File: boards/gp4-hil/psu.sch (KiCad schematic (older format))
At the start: 80 parts, among them K1 CONN_3_PWROUT, Q11 SSM6N58NU, Q12 DMP2069UFY4, Q22 DMP2069UFY4, U1 MIC2288-DFN, U20 SIP32408, U21 SIP32408, U22 SIP32408, U23 SIP32408, U24 SIP32408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

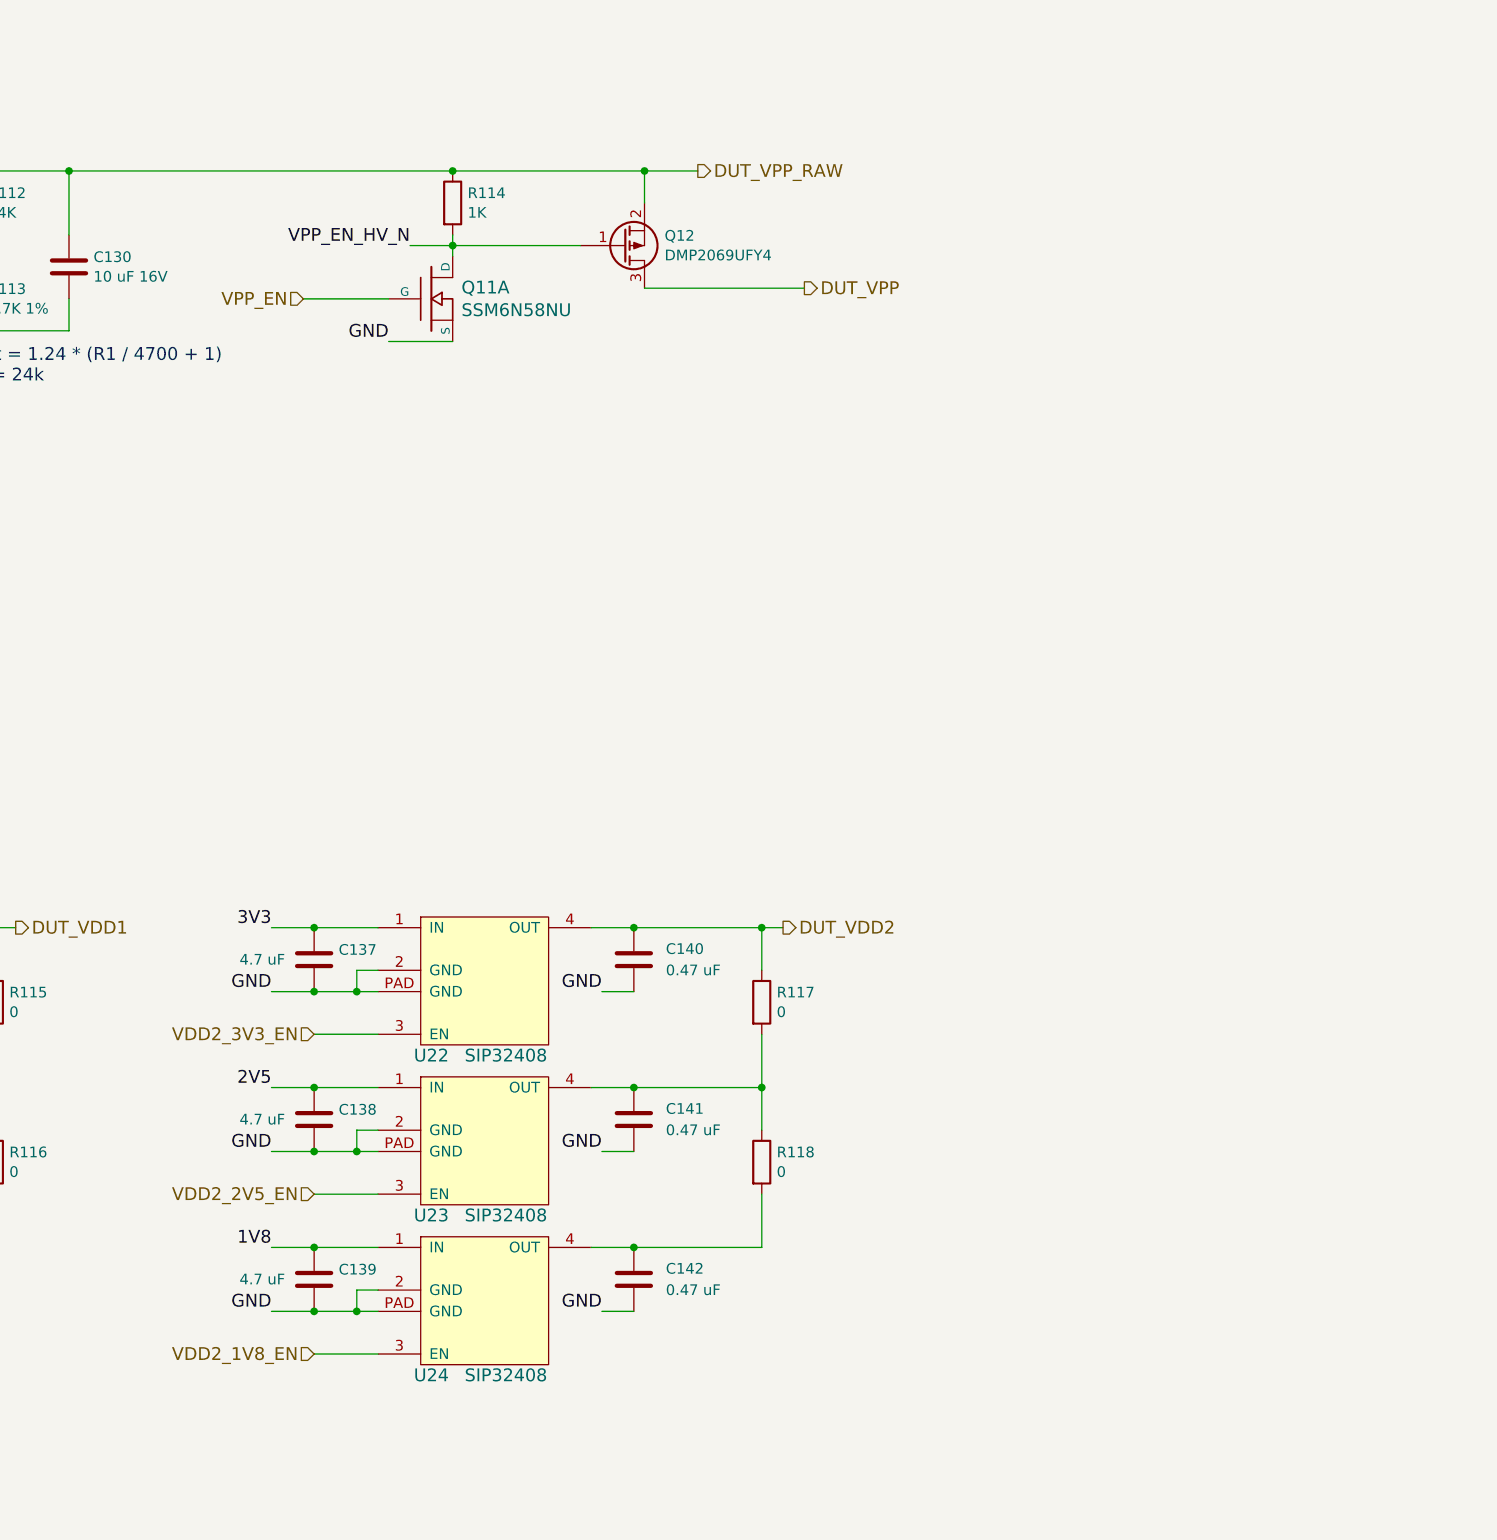
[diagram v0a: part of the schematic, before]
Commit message: Added current monitoring shunts. Began design review
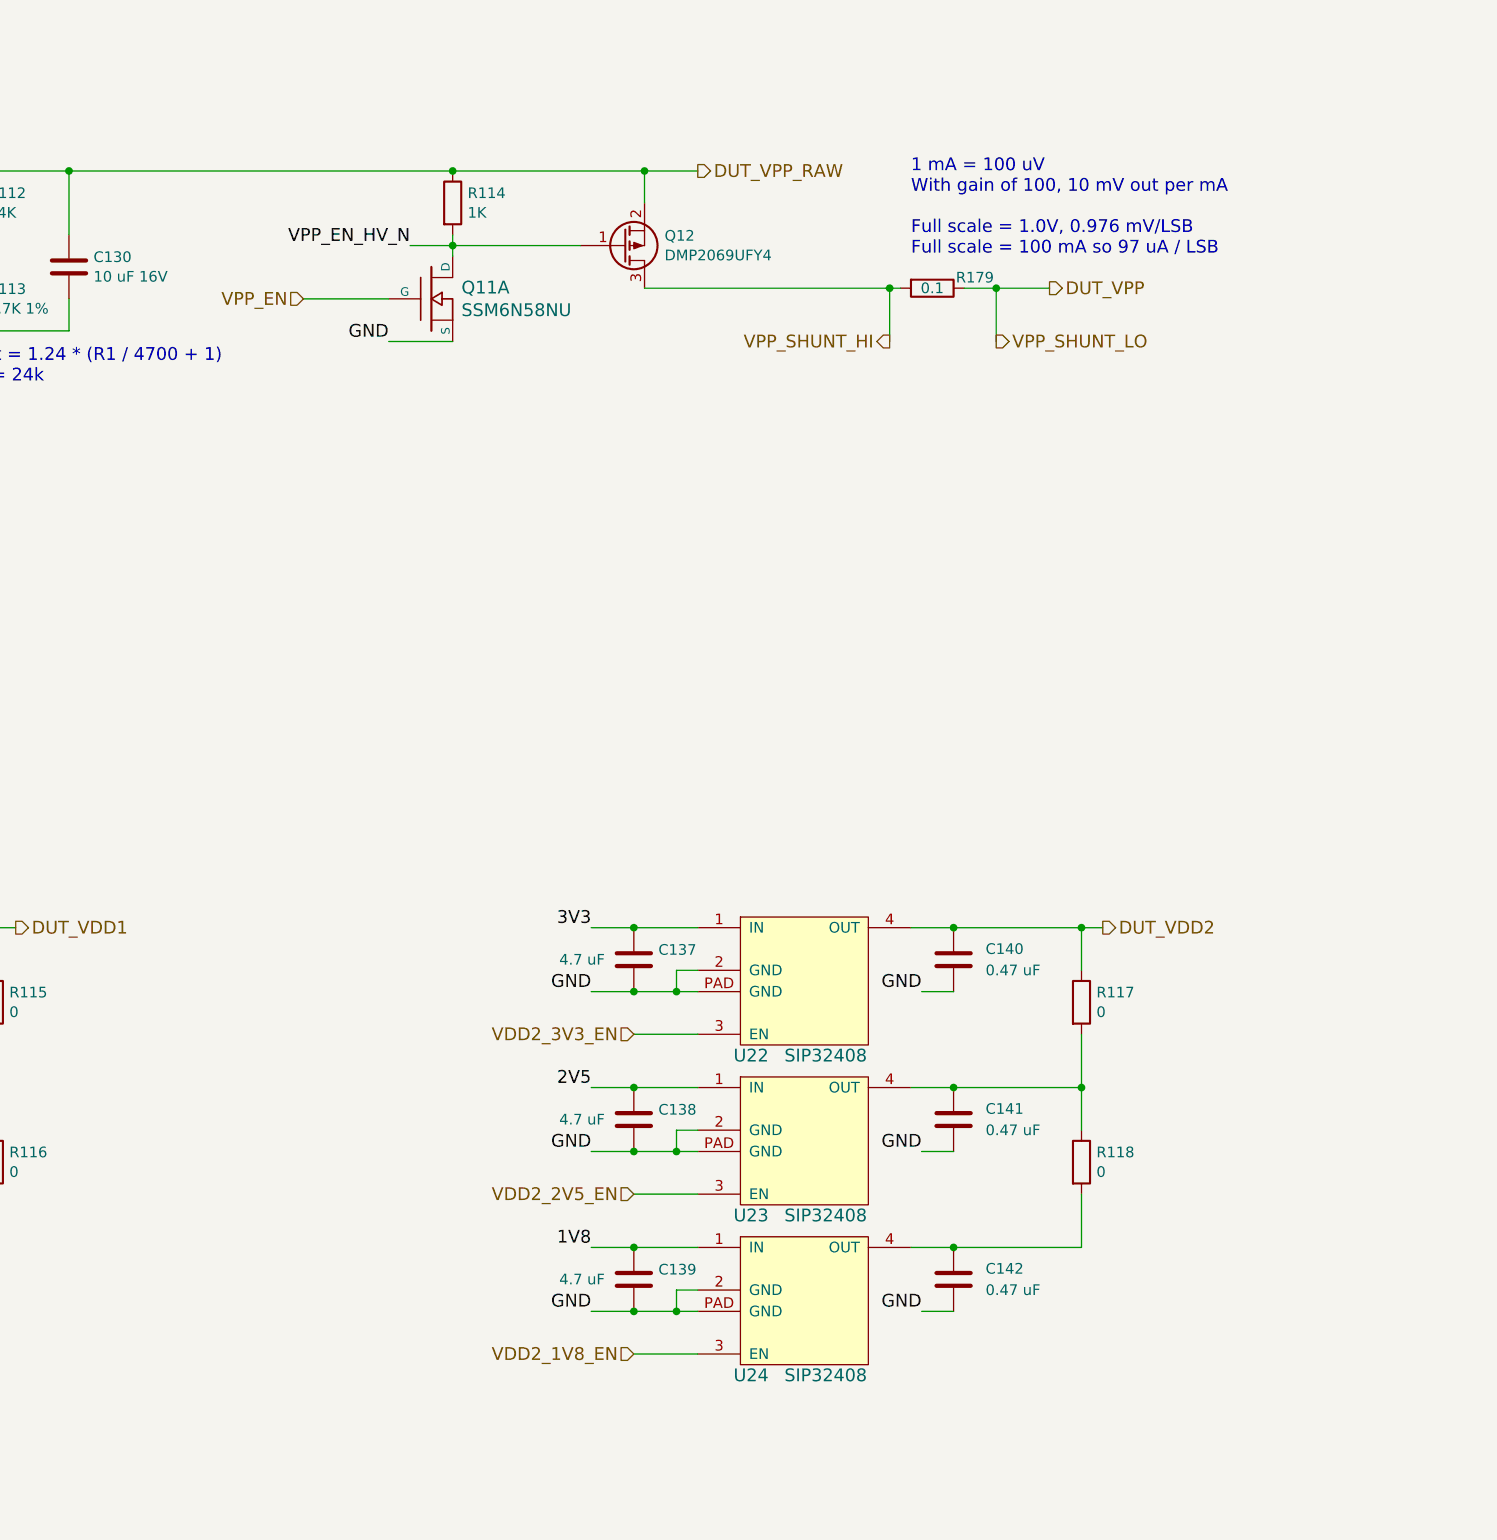
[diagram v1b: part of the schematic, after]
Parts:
- added R179: 0.1, symbol R
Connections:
- net DUT_VPP: now also R179.1; no longer Q12.3 (D)
- new net VPP_SHUNT_HI: Q12.3 (D), R179.2
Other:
- note added: "1 mA = 100 uV\nWith gain of 100, 10 mV out per mA\n\nFull scale = 1.0V, 0.976 mV/LSB\nFull scale = 100 mA so 97 uA / LSB"
- moved on the sheet: C137, C138, C139, C140, C141, C142, R117, R118, U22, U23, U24
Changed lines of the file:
@@
 Sheet 2 7
 Title "GreenPak Hardware-In-Loop Test Platform"
-Date "2016-05-17"
+Date "2016-05-18"
 Rev "0.1"
 Comp "Andrew Zonenberg"
@@
 	-1   0    0    -1
 $EndComp
-Text HLabel 13100 4550 2    60   Output ~ 0
+Text HLabel 14250 4550 2    60   Output ~ 0
 DUT_VPP
 Text HLabel 4550 9500 2    60   Output ~ 0
@@
 Text HLabel 7200 8800 0    60   Input ~ 0
 VDD1_2V5_EN
-Text HLabel 13000 7550 2    60   Output ~ 0
+Text HLabel 14500 7550 2    60   Output ~ 0
 DUT_VDD2
 $Comp
 L SIP32408 U22
 U 1 1 57415A55
-P 11300 8100
-F 0 "U22" H 11350 8050 60  0000 C CNN
-F 1 "SIP32408" H 11700 8050 60  0000 C CNN
-F 2 "" H 11300 8100 60  0000 C CNN
-F 3 "" H 11300 8100 60  0000 C CNN
-	1    11300 8100
+P 12800 8100
+F 0 "U22" H 12850 8050 60  0000 C CNN
+F 1 "SIP32408" H 13200 8050 60  0000 C CNN
+F 2 "" H 12800 8100 60  0000 C CNN
+F 3 "" H 12800 8100 60  0000 C CNN
+	1    12800 8100
 	1    0    0    -1
 $EndComp
@@
 L C C137
 U 1 1 57415A5B
-P 10800 7700
-F 0 "C137" H 10915 7746 50  0000 L CNN
-F 1 "4.7 uF" H 10450 7700 50  0000 L CNN
-F 2 "" H 10838 7550 30  0000 C CNN
-F 3 "" H 10800 7700 60  0000 C CNN
-	1    10800 7700
-	1    0    0    -1
-$EndComp
-Text Label 10600 7850 2    60   ~ 0
-GND
-Text Label 10600 7550 2    60   ~ 0
-3V3
-$Comp
-L C C140
-U 1 1 57415A63
 P 12300 7700
-F 0 "C140" H 12450 7750 50  0000 L CNN
-F 1 "0.47 uF" H 12450 7650 50  0000 L CNN
+F 0 "C137" H 12415 7746 50  0000 L CNN
+F 1 "4.7 uF" H 11950 7700 50  0000 L CNN
 F 2 "" H 12338 7550 30  0000 C CNN
 F 3 "" H 12300 7700 60  0000 C CNN
@@
 	1    0    0    -1
 $EndComp
-Text Label 12150 7850 2    60   ~ 0
-GND
-Text HLabel 10800 8050 0    60   Input ~ 0
+Text Label 12100 7850 2    60   ~ 0
+GND
+Text Label 12100 7550 2    60   ~ 0
+3V3
+$Comp
+L C C140
+U 1 1 57415A63
+P 13800 7700
+F 0 "C140" H 13950 7750 50  0000 L CNN
+F 1 "0.47 uF" H 13950 7650 50  0000 L CNN
+F 2 "" H 13838 7550 30  0000 C CNN
+F 3 "" H 13800 7700 60  0000 C CNN
+	1    13800 7700
+	1    0    0    -1
+$EndComp
+Text Label 13650 7850 2    60   ~ 0
+GND
+Text HLabel 12300 8050 0    60   Input ~ 0
 VDD2_3V3_EN
 $Comp
 L SIP32408 U24
 U 1 1 57415A75
-P 11300 9600
-F 0 "U24" H 11350 9550 60  0000 C CNN
-F 1 "SIP32408" H 11700 9550 60  0000 C CNN
-F 2 "" H 11300 9600 60  0000 C CNN
-F 3 "" H 11300 9600 60  0000 C CNN
-	1    11300 9600
+P 12800 9600
+F 0 "U24" H 12850 9550 60  0000 C CNN
+F 1 "SIP32408" H 13200 9550 60  0000 C CNN
+F 2 "" H 12800 9600 60  0000 C CNN
+F 3 "" H 12800 9600 60  0000 C CNN
+	1    12800 9600
 	1    0    0    -1
 $EndComp
@@
 L C C139
 U 1 1 57415A7B
-P 10800 9200
-F 0 "C139" H 10915 9246 50  0000 L CNN
-F 1 "4.7 uF" H 10450 9200 50  0000 L CNN
-F 2 "" H 10838 9050 30  0000 C CNN
-F 3 "" H 10800 9200 60  0000 C CNN
-	1    10800 9200
-	1    0    0    -1
-$EndComp
-Text Label 10600 9350 2    60   ~ 0
-GND
-Text Label 10600 9050 2    60   ~ 0
-1V8
-$Comp
-L C C142
-U 1 1 57415A83
 P 12300 9200
-F 0 "C142" H 12450 9250 50  0000 L CNN
-F 1 "0.47 uF" H 12450 9150 50  0000 L CNN
+F 0 "C139" H 12415 9246 50  0000 L CNN
+F 1 "4.7 uF" H 11950 9200 50  0000 L CNN
 F 2 "" H 12338 9050 30  0000 C CNN
 F 3 "" H 12300 9200 60  0000 C CNN
@@
 	1    0    0    -1
 $EndComp
-Text Label 12150 9350 2    60   ~ 0
-GND
-Text HLabel 10800 9550 0    60   Input ~ 0
+Text Label 12100 9350 2    60   ~ 0
+GND
+Text Label 12100 9050 2    60   ~ 0
+1V8
+$Comp
+L C C142
+U 1 1 57415A83
+P 13800 9200
+F 0 "C142" H 13950 9250 50  0000 L CNN
+F 1 "0.47 uF" H 13950 9150 50  0000 L CNN
+F 2 "" H 13838 9050 30  0000 C CNN
+F 3 "" H 13800 9200 60  0000 C CNN
+	1    13800 9200
+	1    0    0    -1
+$EndComp
+Text Label 13650 9350 2    60   ~ 0
+GND
+Text HLabel 12300 9550 0    60   Input ~ 0
 VDD2_1V8_EN
 $Comp
 L SIP32408 U23
 U 1 1 57415A95
-P 11300 8850
-F 0 "U23" H 11350 8800 60  0000 C CNN
-F 1 "SIP32408" H 11700 8800 60  0000 C CNN
-F 2 "" H 11300 8850 60  0000 C CNN
-F 3 "" H 11300 8850 60  0000 C CNN
-	1    11300 8850
+P 12800 8850
+F 0 "U23" H 12850 8800 60  0000 C CNN
+F 1 "SIP32408" H 13200 8800 60  0000 C CNN
+F 2 "" H 12800 8850 60  0000 C CNN
+F 3 "" H 12800 8850 60  0000 C CNN
+	1    12800 8850
 	1    0    0    -1
 $EndComp
@@
 L C C138
 U 1 1 57415A9B
-P 10800 8450
-F 0 "C138" H 10915 8496 50  0000 L CNN
-F 1 "4.7 uF" H 10450 8450 50  0000 L CNN
-F 2 "" H 10838 8300 30  0000 C CNN
-F 3 "" H 10800 8450 60  0000 C CNN
-	1    10800 8450
-	1    0    0    -1
-$EndComp
-Text Label 10600 8600 2    60   ~ 0
-GND
-Text Label 10600 8300 2    60   ~ 0
-2V5
-$Comp
-L C C141
-U 1 1 57415AA3
 P 12300 8450
-F 0 "C141" H 12450 8500 50  0000 L CNN
-F 1 "0.47 uF" H 12450 8400 50  0000 L CNN
+F 0 "C138" H 12415 8496 50  0000 L CNN
+F 1 "4.7 uF" H 11950 8450 50  0000 L CNN
 F 2 "" H 12338 8300 30  0000 C CNN
 F 3 "" H 12300 8450 60  0000 C CNN
@@
 	1    0    0    -1
 $EndComp
-Text Label 12150 8600 2    60   ~ 0
-GND
-Text HLabel 10800 8800 0    60   Input ~ 0
+Text Label 12100 8600 2    60   ~ 0
+GND
+Text Label 12100 8300 2    60   ~ 0
+2V5
+$Comp
+L C C141
+U 1 1 57415AA3
+P 13800 8450
+F 0 "C141" H 13950 8500 50  0000 L CNN
+F 1 "0.47 uF" H 13950 8400 50  0000 L CNN
+F 2 "" H 13838 8300 30  0000 C CNN
+F 3 "" H 13800 8450 60  0000 C CNN
+	1    13800 8450
+	1    0    0    -1
+$EndComp
+Text Label 13650 8600 2    60   ~ 0
+GND
+Text HLabel 12300 8800 0    60   Input ~ 0
 VDD2_2V5_EN
 Text HLabel 10750 4600 0    60   Input ~ 0
@@
 L R R117
 U 1 1 574582F9
-P 12900 7900
-F 0 "R117" H 12970 7946 50  0000 L CNN
-F 1 "0" H 12970 7854 50  0000 L CNN
-F 2 "" V 12830 7900 30  0000 C CNN
-F 3 "" H 12900 7900 30  0000 C CNN
-	1    12900 7900
+P 14400 7900
+F 0 "R117" H 14470 7946 50  0000 L CNN
+F 1 "0" H 14470 7854 50  0000 L CNN
+F 2 "" V 14330 7900 30  0000 C CNN
+F 3 "" H 14400 7900 30  0000 C CNN
+	1    14400 7900
 	1    0    0    -1
 $EndComp
@@
 L R R118
 U 1 1 5745846F
-P 12900 8650
-F 0 "R118" H 12970 8696 50  0000 L CNN
-F 1 "0" H 12970 8604 50  0000 L CNN
-F 2 "" V 12830 8650 30  0000 C CNN
-F 3 "" H 12900 8650 30  0000 C CNN
-	1    12900 8650
+P 14400 8650
+F 0 "R118" H 14470 8696 50  0000 L CNN
+F 1 "0" H 14470 8604 50  0000 L CNN
+F 2 "" V 14330 8650 30  0000 C CNN
+F 3 "" H 14400 8650 30  0000 C CNN
+	1    14400 8650
 	1    0    0    -1
 $EndComp
@@
 	1    0    0    -1
 $EndComp
+Text Label 4200 15950 2    60   ~ 0
+GND
 Wire Wire Line
 	1650 15100 2300 15100
@@
 Connection ~ 8700 9050
 Wire Wire Line
-	10600 7550 11100 7550
-Wire Wire Line
-	10600 7850 11100 7850
-Wire Wire Line
-	11100 7750 11000 7750
-Wire Wire Line
-	11000 7750 11000 7850
-Connection ~ 11000 7850
-Connection ~ 10800 7850
-Connection ~ 10800 7550
-Wire Wire Line
-	12100 7550 13000 7550
-Wire Wire Line
-	12150 7850 12300 7850
-Wire Wire Line
-	10800 8050 11100 8050
-Wire Wire Line
-	10600 9050 11100 9050
-Wire Wire Line
-	10600 9350 11100 9350
-Wire Wire Line
-	11100 9250 11000 9250
-Wire Wire Line
-	11000 9250 11000 9350
-Connection ~ 11000 9350
-Connection ~ 10800 9350
-Connection ~ 10800 9050
-Wire Wire Line
-	12900 9050 12100 9050
-Wire Wire Line
-	12150 9350 12300 9350
-Wire Wire Line
-	10800 9550 11100 9550
-Wire Wire Line
-	10600 8300 11100 8300
-Wire Wire Line
-	10600 8600 11100 8600
-Wire Wire Line
-	11100 8500 11000 8500
-Wire Wire Line
-	11000 8500 11000 8600
-Connection ~ 11000 8600
-Connection ~ 10800 8600
-Connection ~ 10800 8300
-Wire Wire Line
-	12100 8300 12900 8300
-Wire Wire Line
-	12150 8600 12300 8600
-Wire Wire Line
-	10800 8800 11100 8800
+	12100 7550 12600 7550
+Wire Wire Line
+	12100 7850 12600 7850
+Wire Wire Line
+	12600 7750 12500 7750
+Wire Wire Line
+	12500 7750 12500 7850
+Connection ~ 12500 7850
+Connection ~ 12300 7850
 Connection ~ 12300 7550
-Connection ~ 12900 7550
+Wire Wire Line
+	13600 7550 14500 7550
+Wire Wire Line
+	13650 7850 13800 7850
+Wire Wire Line
+	12300 8050 12600 8050
+Wire Wire Line
+	12100 9050 12600 9050
+Wire Wire Line
+	12100 9350 12600 9350
+Wire Wire Line
+	12600 9250 12500 9250
+Wire Wire Line
+	12500 9250 12500 9350
+Connection ~ 12500 9350
+Connection ~ 12300 9350
+Connection ~ 12300 9050
+Wire Wire Line
+	14400 9050 13600 9050
+Wire Wire Line
+	13650 9350 13800 9350
+Wire Wire Line
+	12300 9550 12600 9550
+Wire Wire Line
+	12100 8300 12600 8300
+Wire Wire Line
+	12100 8600 12600 8600
+Wire Wire Line
+	12600 8500 12500 8500
+Wire Wire Line
+	12500 8500 12500 8600
+Connection ~ 12500 8600
+Connection ~ 12300 8600
 Connection ~ 12300 8300
-Connection ~ 12900 8300
-Connection ~ 12300 9050
+Wire Wire Line
+	13600 8300 14400 8300
+Wire Wire Line
+	13650 8600 13800 8600
+Wire Wire Line
+	12300 8800 12600 8800
+Connection ~ 13800 7550
+Connection ~ 14400 7550
+Connection ~ 13800 8300
+Connection ~ 14400 8300
+Connection ~ 13800 9050
 Wire Wire Line
 	11450 4300 11450 4400
@@
 Connection ~ 11450 4000
 Wire Wire Line
-	13100 4550 12350 4550
+	12350 4550 13550 4550
 Wire Wire Line
 	9300 9050 9300 8800
@@
 Connection ~ 9250 7550
 Wire Wire Line
-	12900 9050 12900 8800
-Wire Wire Line
-	12900 8050 12900 8500
-Wire Wire Line
-	12900 7550 12900 7750
+	14400 9050 14400 8800
+Wire Wire Line
+	14400 8050 14400 8500
+Wire Wire Line
+	14400 7550 14400 7750
 Connection ~ 1600 1650
 Connection ~ 1050 1650
@@
 Wire Wire Line
 	4400 15500 4400 15550
-Text Label 4200 15950 2    60   ~ 0
-GND
 Wire Wire Line
 	4200 15950 4400 15950
+Wire Wire Line
+	13850 4550 14250 4550
+Text Notes 13600 4400 0    60   ~ 0
+1 mA = 100 uV\nWith gain of 100, 10 mV out per mA\n\nFull scale = 1.0V, 0.976 mV/LSB\nFull scale = 100 mA so 97 uA / LSB
+$Comp
+L R R179
+U 1 1 57690956
+P 13700 4550
+F 0 "R179" V 13650 4750 50  0000 C CNN
+F 1 "0.1" V 13700 4550 50  0000 C CNN
+F 2 "" V 13630 4550 30  0000 C CNN
+F 3 "" H 13700 4550 30  0000 C CNN
+	1    13700 4550
+	0    1    1    0
+$EndComp
+Text HLabel 13500 4800 0    60   Output ~ 0
+VPP_SHUNT_HI
+Text HLabel 14000 4800 2    60   Output ~ 0
+VPP_SHUNT_LO
+Wire Wire Line
+	14000 4800 14000 4550
+Connection ~ 14000 4550
+Wire Wire Line
+	13500 4800 13500 4550
+Connection ~ 13500 4550
 $EndSCHEMATC

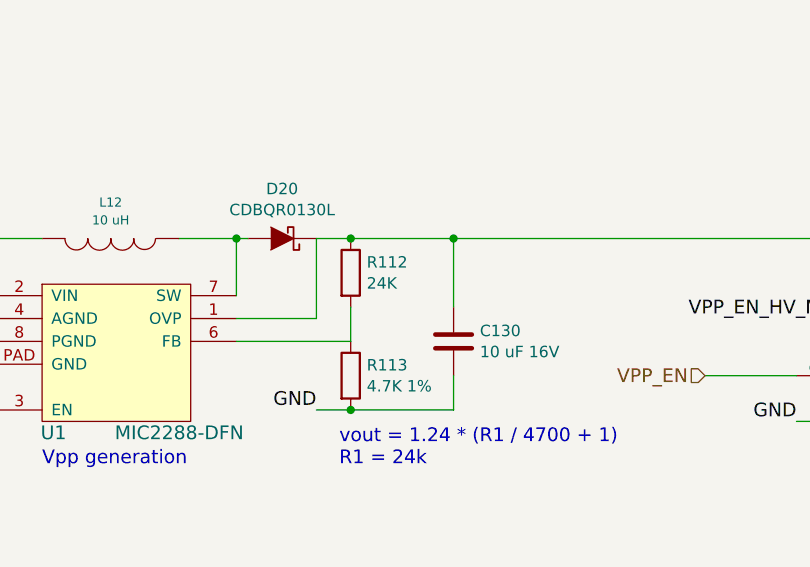
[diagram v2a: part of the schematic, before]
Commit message: Minor refdes placement tweaks
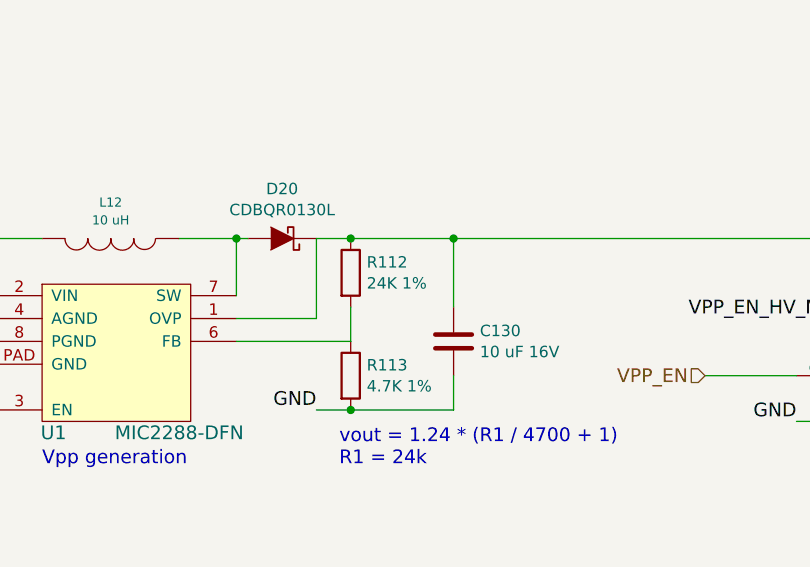
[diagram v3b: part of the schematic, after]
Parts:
- R112: value 24K -> 24K 1%
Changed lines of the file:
@@
 P 9200 4150
 F 0 "R112" H 9270 4196 50  0000 L CNN
-F 1 "24K" H 9270 4104 50  0000 L CNN
+F 1 "24K 1%" H 9270 4104 50  0000 L CNN
 F 2 "" V 9130 4150 30  0000 C CNN
 F 3 "" H 9200 4150 30  0000 C CNN
